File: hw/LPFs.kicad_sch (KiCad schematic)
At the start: 28 parts, among them K201 G6K-2, K202 G6K-2, K203 G6K-2, Q201 MMBF170, Q202 MMBF170, Q203 MMBF170

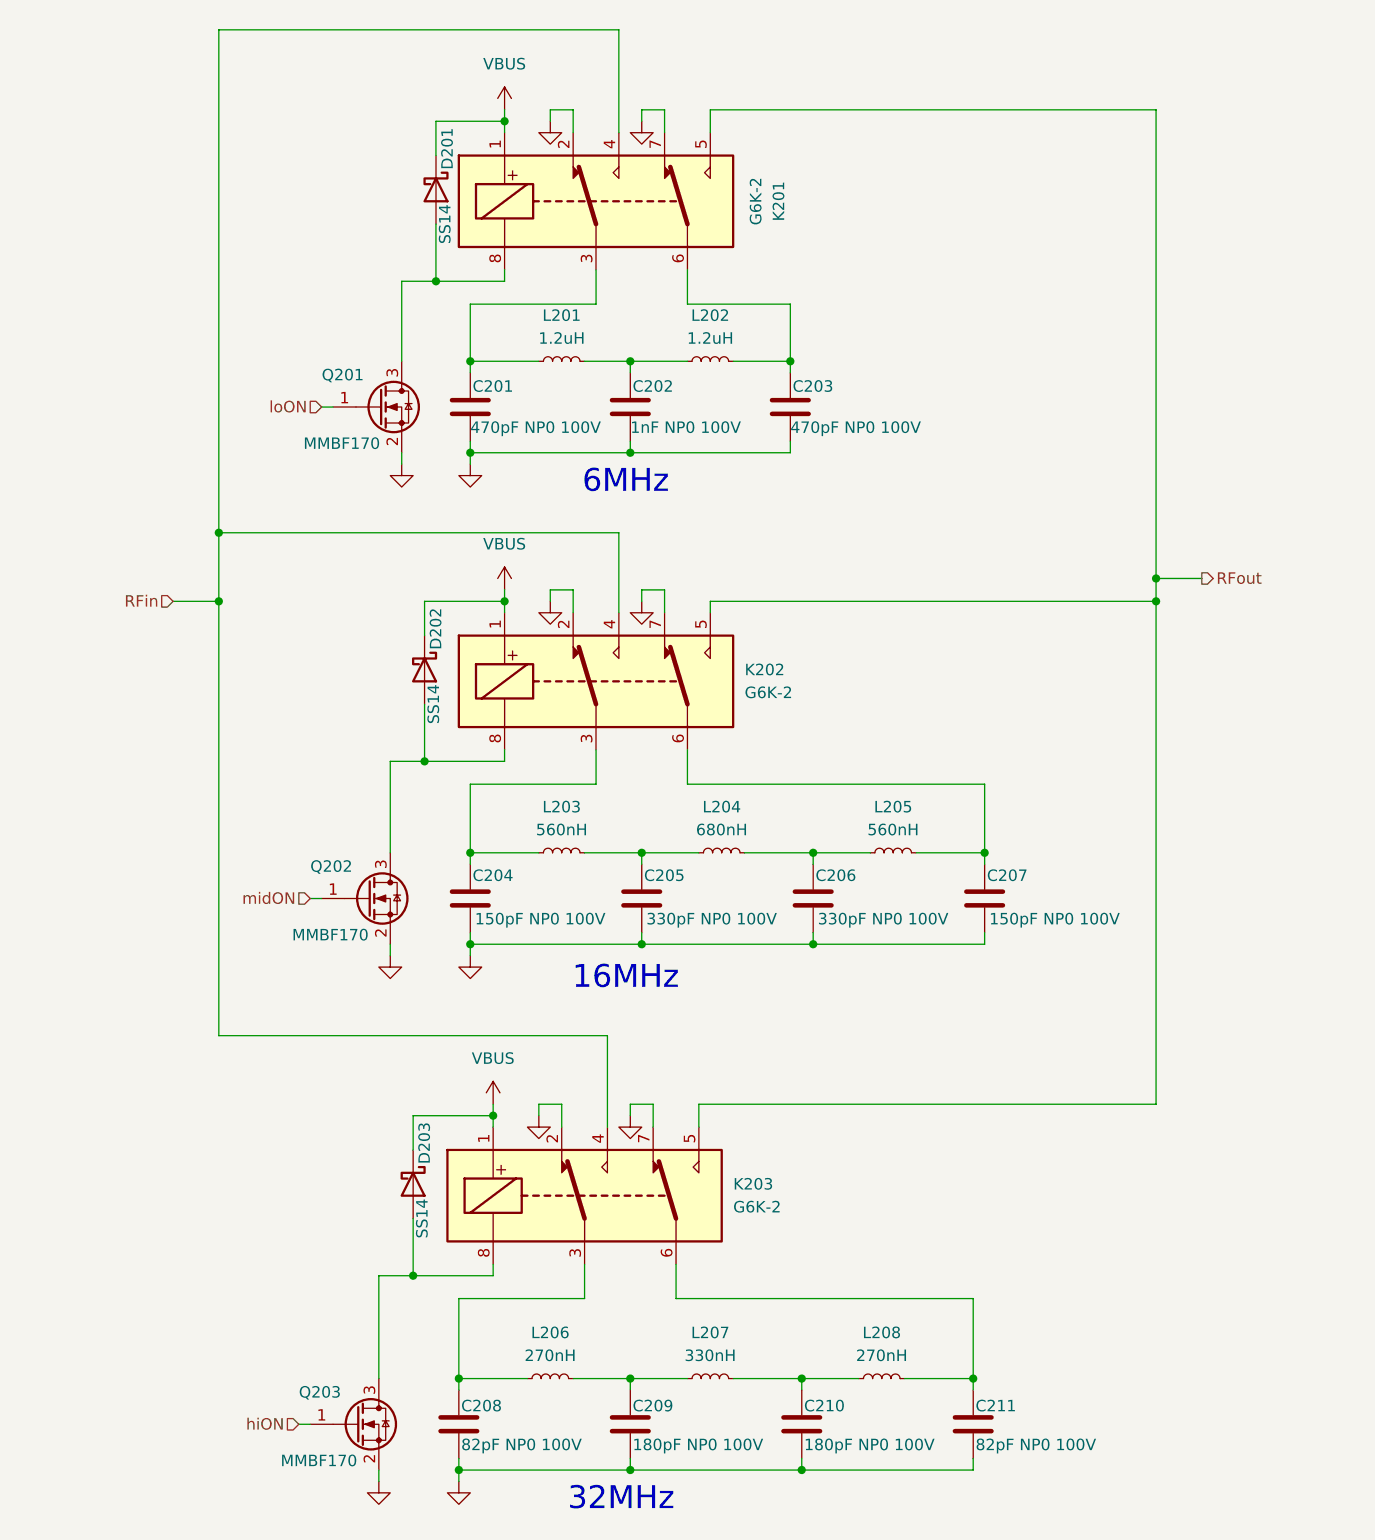
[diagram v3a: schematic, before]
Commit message: Add symbols for new components, switch to SI5351 in place of FPGA. Simplify!
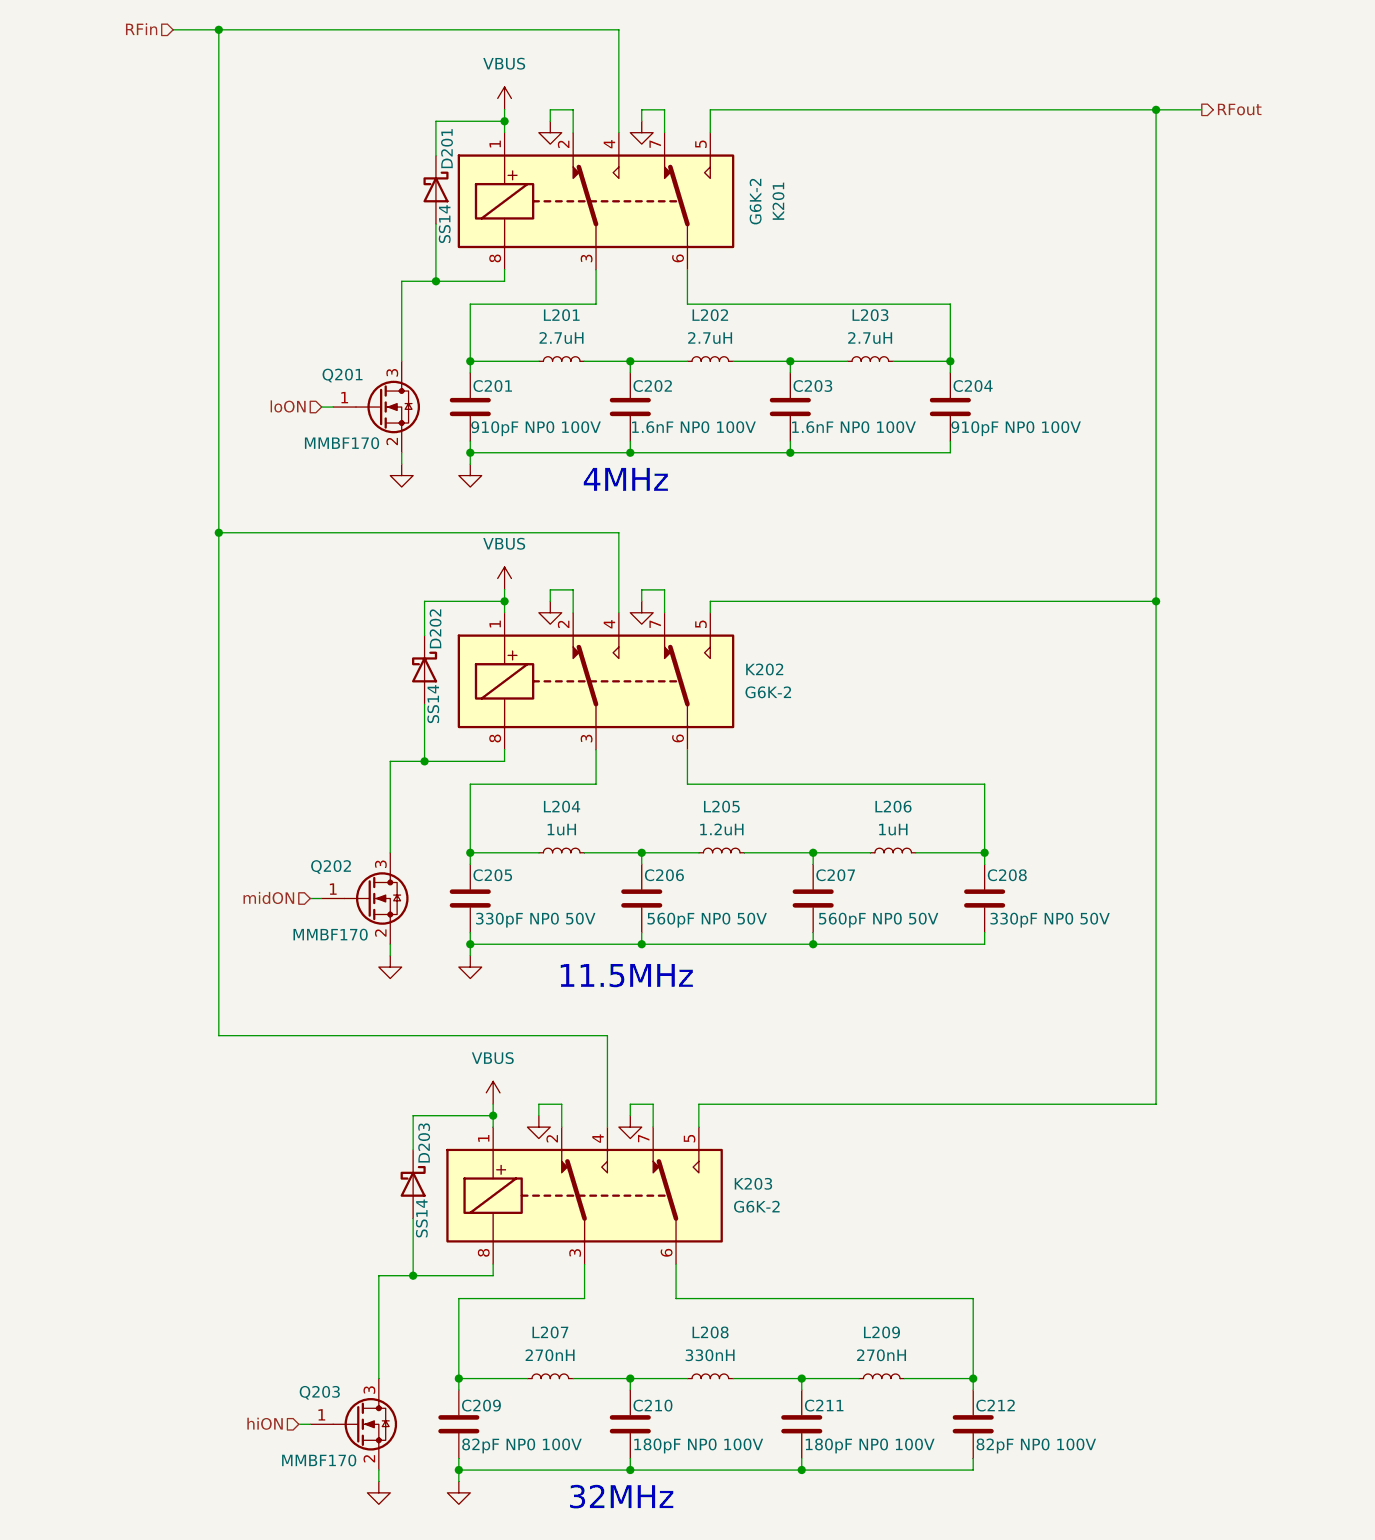
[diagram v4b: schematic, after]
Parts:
- removed C206: 330pF NP0 100V, Capacitor_SMD:C_0603_1608Metric, symbol Device:C
- removed L205: 560nH, Inductor_SMD:L_1008_2520Metric, symbol Device:L_Small
- added C204: 910pF NP0 100V, Capacitor_SMD:C_0603_1608Metric, symbol Device:C
- added C208: 330pF NP0 50V, Capacitor_SMD:C_0603_1608Metric, symbol Device:C
- added L203: 2.7uH, Inductor_SMD:L_1008_2520Metric, symbol Device:L_Small
- added L206: 1uH, Inductor_SMD:L_1008_2520Metric, symbol Device:L_Small
- C201: value 470pF NP0 100V -> 910pF NP0 100V; MPN GCM1885C2A471FA6D -> GCM1885C2A911FA16D; Mouser_PN 81-GCM1885C2A471FA6D -> 81-GCM1885C2A911FA6D
- C202: value 1nF NP0 100V -> 1.6nF NP0 100V; MFG Kyocera AVX -> muRata; MPN KGM15ACG2A102FT -> GCM1885C1J162JA16D; Mouser_PN 581-KGM15ACG2A102FT -> 81-GCM1885C1J162JA6D
- C203: value 470pF NP0 100V -> 1.6nF NP0 100V; LCSC C106259 -> C5182455; MPN GCM1885C2A471FA6D -> GCM1885C1J162JA16D; Mouser_PN 81-GCM1885C2A471FA6D -> 81-GCM1885C1J162JA6D; cap-type (none) -> X5R; working-voltage (none) -> 25V
- C205: renamed from C204; value 150pF NP0 100V -> 330pF NP0 50V; LCSC C107001 -> (none); MPN GRM1885C2A151JA01D -> GRM1885C1H331JA01D; Mouser_PN 81-GRM1885C2A151JA01 -> 81-GRM39C331J50
- C206: renamed from C205; value 330pF NP0 100V -> 560pF NP0 50V; LCSC C106259 -> (none); MPN GRM1885C2A331JA01D -> GRM1885C1H561JA01D; Mouser_PN 81-GRM185C2A331JA01D -> 81-GRM39C561J50
- C207: value 150pF NP0 100V -> 560pF NP0 50V; LCSC C107001 -> (none); MPN GRM1885C2A151JA01D -> GRM1885C1H561JA01D; Mouser_PN 81-GRM1885C2A151JA01 -> 81-GRM39C561J50
- L201, L202: value 1.2uH -> 2.7uH; LCSC C2044063 -> (none); MPN 1008LS-122XJR -> 1008LS-272XJRC; Manufacturer_Name Coilcraft -> (none); Mouser_PN 652-CW252016-1R2J -> 994-1008LS-272XJRC
- L204: renamed from L203; value 560nH -> 1uH; MPN 1008CS-561XJRC -> 1008CS-102XJRC; Mouser_PN 994-1008CS-561XJRC -> 994-1008CS-102XJRC
- L205: renamed from L204; value 680nH -> 1.2uH; LCSC C6364717 -> (none); MPN 1008CS-681XJRC -> 1008CS-122XJRC; Mouser_PN 994-1008CS-681XJRC -> 994-1008CS-122XJRC
- renumbered C208 to C209, C209 to C210, C210 to C211, C211 to C212, L206 to L207, L207 to L208, L208 to L209
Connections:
- net GND: now also C204.2, C208.2
- net at C203.1, L202.2: now also L203.1; no longer K201.6
- net at L205.2: now also C207.1, L206.1
- net at K202.6: now also C208.1, L206.2; no longer C207.1
- new net: C204.1, K201.6, L203.2
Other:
- note added: "11.5MHz"
- note added: "4MHz"
- note removed: "16MHz"
- note removed: "6MHz"

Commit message: Horsing around with JLCPCB assembly and BOM. I think it is still too expensive to do it this way for p1 build
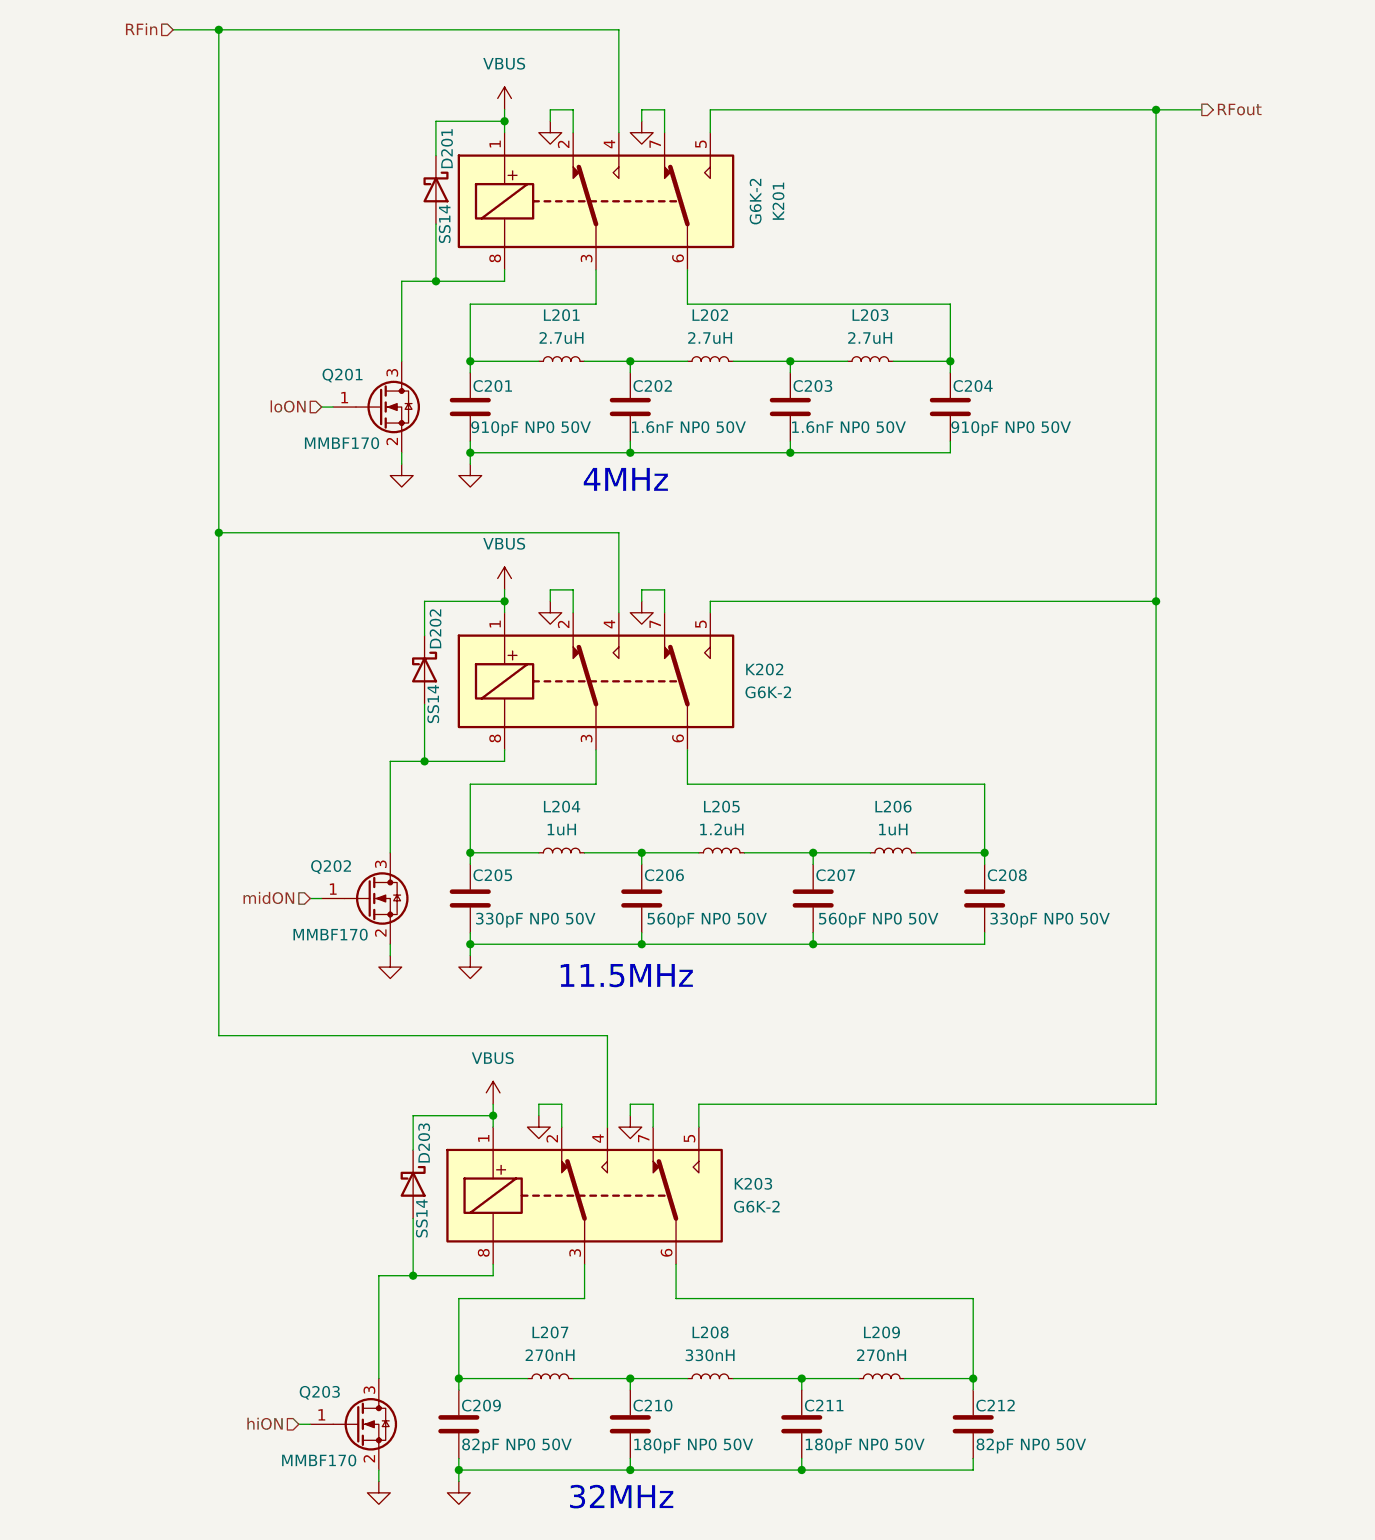
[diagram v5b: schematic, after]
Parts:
- C201, C204: value 910pF NP0 100V -> 910pF NP0 50V; LCSC C106259 -> C2941944; cap-type (none) -> NP0; working-voltage (none) -> 50V
- C202, C203: value 1.6nF NP0 100V -> 1.6nF NP0 50V; LCSC C5182455 -> C7471455; cap-type X5R -> NP0; working-voltage 25V -> 50V
- C205, C208: LCSC (none) -> C2176790; cap-type (none) -> NP0; working-voltage (none) -> 50V
- C206, C207: LCSC (none) -> C597173; cap-type (none) -> NP0; working-voltage (none) -> 50V
- C209, C212: value 82pF NP0 100V -> 82pF NP0 50V; LCSC C106200 -> C314304; cap-type (none) -> NP0; working-voltage (none) -> 50V
- C210: value 180pF NP0 100V -> 180pF NP0 50V; LCSC C107001 -> C440147; cap-type (none) -> NP0; working-voltage (none) -> 50V
- C211: value 180pF NP0 100V -> 180pF NP0 50V; LCSC C106200 -> C440147; cap-type (none) -> NP0; working-voltage (none) -> 50V
- D201, D202, D203: LCSC C83852 -> C45406502
- K201, K202, K203: LCSC (none) -> C1525301
- L201, L202, L203: LCSC (none) -> C38121966
- L204, L206: LCSC (none) -> C7159440
- L205: LCSC (none) -> C6364739
- L207, L209: LCSC C404430 -> C48946576
- L208: LCSC C404430 -> C48946577
- Q201, Q202, Q203: LCSC C28871 -> C151058

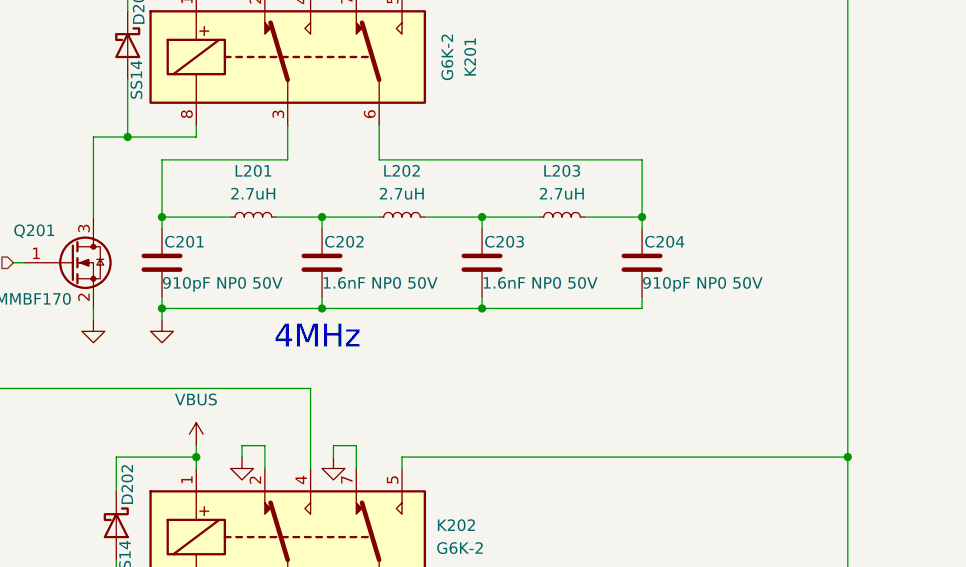
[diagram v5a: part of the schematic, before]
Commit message: OCD fixes. Fix USB2 connector footprint AGAIN (these things are not standardized!).
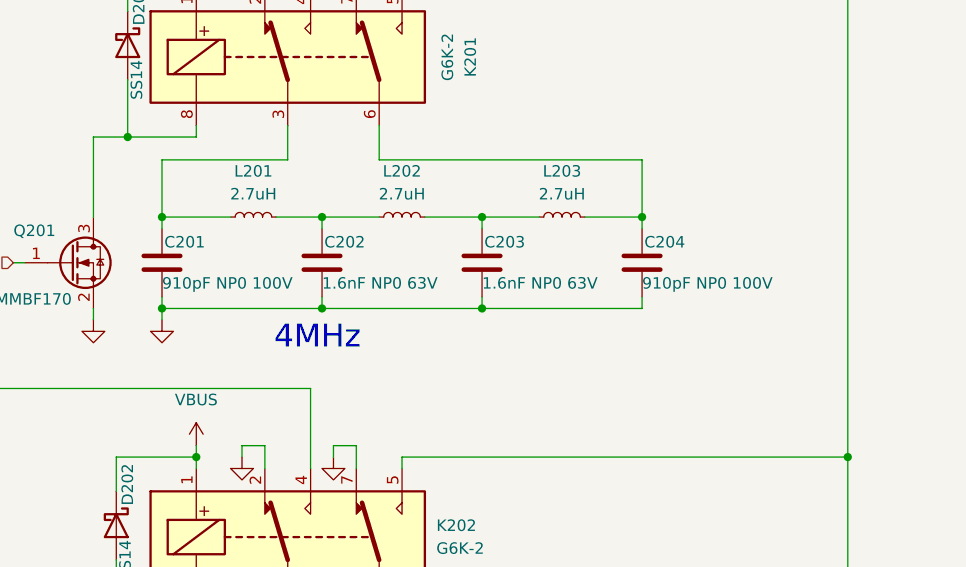
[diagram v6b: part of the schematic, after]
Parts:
- C201, C204: value 910pF NP0 50V -> 910pF NP0 100V; Mouser_PN 81-GCM1885C2A911FA6D -> 81-GCM1885C2A911FA6D
- C202, C203: value 1.6nF NP0 50V -> 1.6nF NP0 63V
- C209, C212: MPN KGM15ACG2A101FT -> KGM15ACG1H820FT; Mouser_PN 581-KGM15ACG2A101FT -> 581-KGM15ACG1H820FT
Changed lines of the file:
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@@
 			)
 		)
-		(property "Value" "910pF NP0 50V"
+		(property "Value" "910pF NP0 100V"
 			(at 137.16 60.706 0)
 			(effects
@@
 			)
 		)
-		(property "Mouser_PN" "81-GCM1885C2A911FA6D"
+		(property "Mouser_PN" "81-GCM1885C2A911FA6D "
 			(at 137.16 58.42 0)
 			(effects
@@
 			)
 		)
-		(property "MPN" "KGM15ACG2A101FT"
+		(property "MPN" "KGM15ACG1H820FT "
 			(at 82.55 171.45 0)
 			(effects
@@
 			)
 		)
-		(property "Mouser_PN" "581-KGM15ACG2A101FT"
+		(property "Mouser_PN" "581-KGM15ACG1H820FT "
 			(at 82.55 171.45 0)
 			(effects
@@
 			)
 		)
-		(property "MPN" "KGM15ACG2A101FT"
+		(property "MPN" "KGM15ACG1H820FT "
 			(at 139.7 171.45 0)
 			(effects
@@
 			)
 		)
-		(property "Mouser_PN" "581-KGM15ACG2A101FT"
+		(property "Mouser_PN" "581-KGM15ACG1H820FT "
 			(at 139.7 171.45 0)
 			(effects
@@
 			)
 		)
-		(property "Value" "1.6nF NP0 50V"
+		(property "Value" "1.6nF NP0 63V"
 			(at 101.6 60.706 0)
 			(effects
@@
 			)
 		)
-		(property "Value" "1.6nF NP0 50V"
+		(property "Value" "1.6nF NP0 63V"
 			(at 119.38 60.706 0)
 			(effects
@@
 			)
 		)
-		(property "Value" "910pF NP0 50V"
+		(property "Value" "910pF NP0 100V"
 			(at 83.82 60.706 0)
 			(effects
@@
 			)
 		)
-		(property "Mouser_PN" "81-GCM1885C2A911FA6D"
+		(property "Mouser_PN" "81-GCM1885C2A911FA6D "
 			(at 83.82 58.42 0)
 			(effects
